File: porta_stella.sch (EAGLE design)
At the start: 85 parts, among them IC1 74LS00D, T1 2N3904, T2 PN3906, T3 PN3906, T4 PN3906, X1 SSW-112-02-G-Q

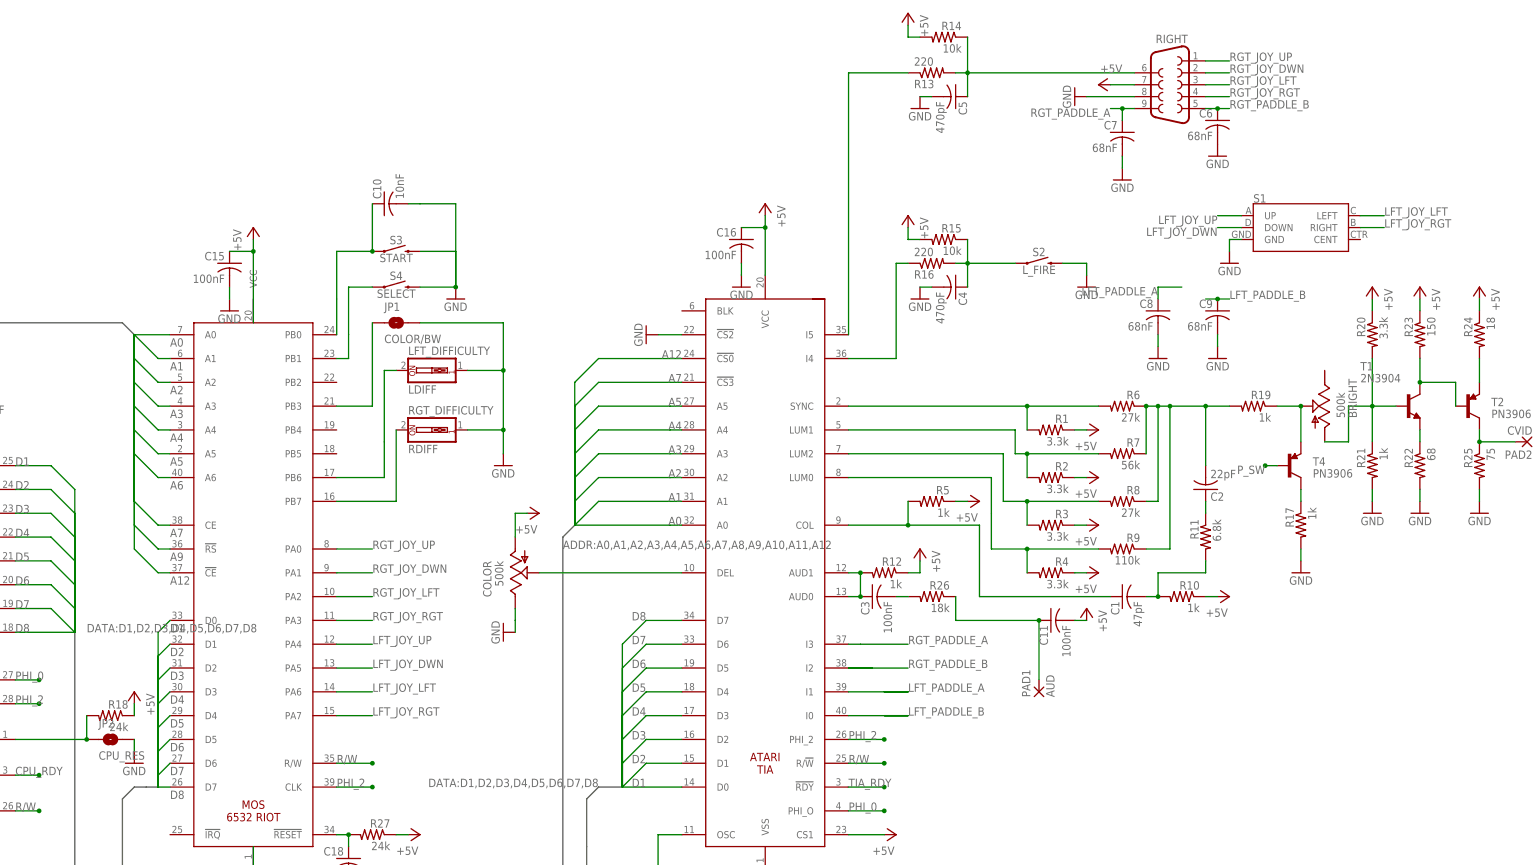
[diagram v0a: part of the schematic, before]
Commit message: more layout work for handheld
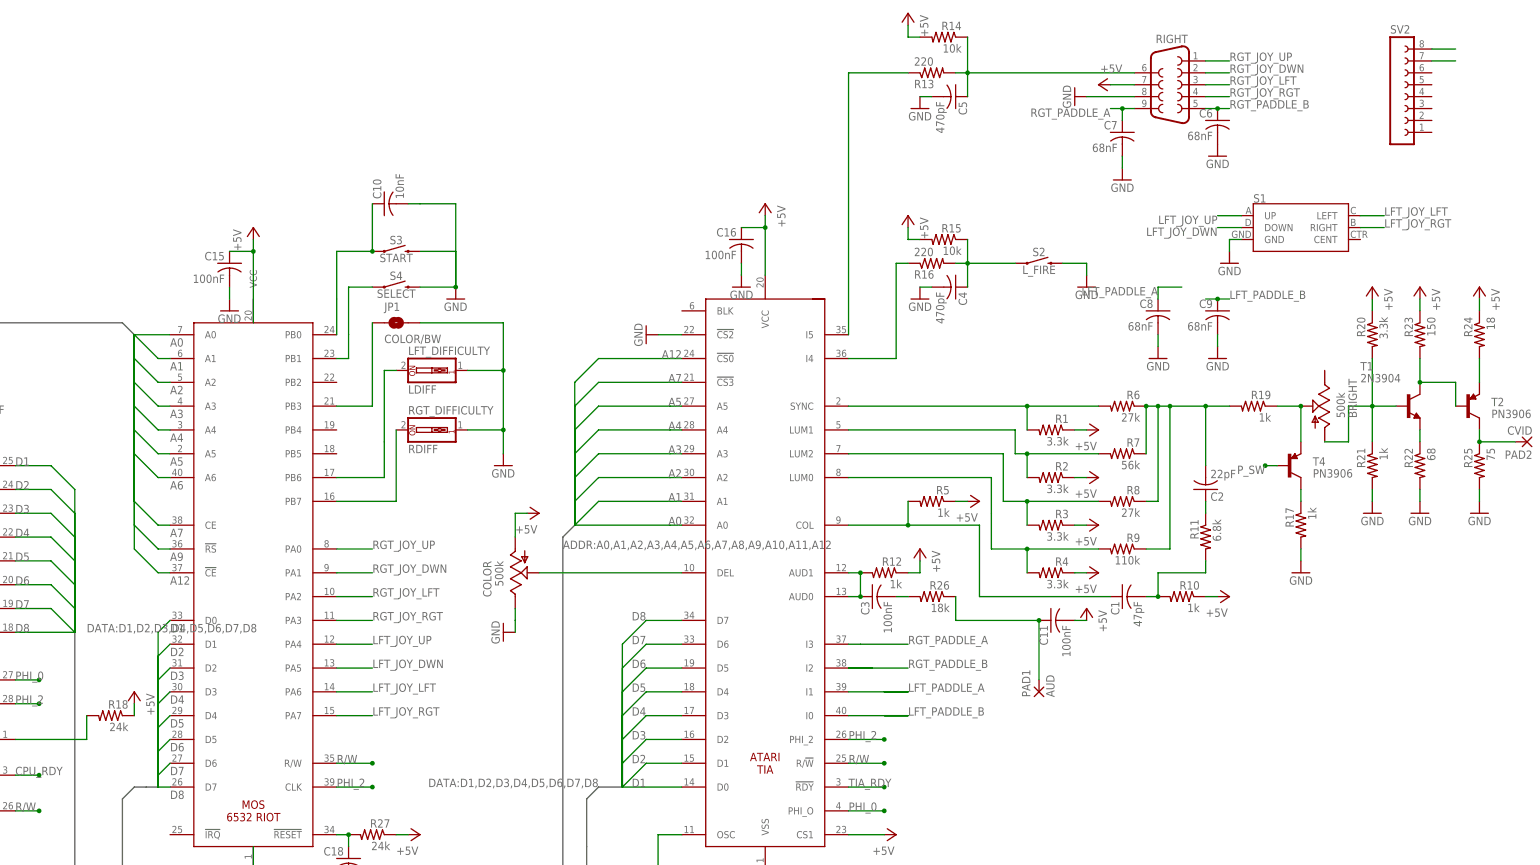
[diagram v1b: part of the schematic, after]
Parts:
- removed JP2: CPU_RES, SparkFun-Jumpers:JUMPER-SMT_2_NO_NO-SILK
- added SV2: (no value), con-lsta:FE08-1
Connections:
- new net N$37: SV2.8
- new net N$41: SV2.7
- net GND: no longer JP2.2
- net N$23: no longer JP2.1
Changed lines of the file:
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@@
 <part name="LDIFF" library="special" library_urn="urn:adsk.eagle:library:367" deviceset="SW_DIP-1" device="" package3d_urn="urn:adsk.eagle:package:26661/1" value="LFT_DIFFICULTY"/>
 <part name="GND17" library="supply1" library_urn="urn:adsk.eagle:library:371" deviceset="GND" device=""/>
-<part name="JP2" library="SparkFun-Jumpers" library_urn="urn:adsk.eagle:library:528" deviceset="JUMPER-SMT_2_NO" device="_NO-SILK" package3d_urn="urn:adsk.eagle:package:39277/1" value="CPU_RES"/>
-<part name="GND18" library="supply1" library_urn="urn:adsk.eagle:library:371" deviceset="GND" device=""/>
 <part name="R18" library="resistor" library_urn="urn:adsk.eagle:library:348" deviceset="R-US_" device="M0805" package3d_urn="urn:adsk.eagle:package:26079/1" value="24k"/>
 <part name="P+14" library="supply1" library_urn="urn:adsk.eagle:library:371" deviceset="+5V" device=""/>
@@
 <part name="PAD1" library="wirepad" library_urn="urn:adsk.eagle:library:412" deviceset="WIREPAD" device="4,16O1,6" package3d_urn="urn:adsk.eagle:package:30843/1" value="AUD"/>
 <part name="PAD2" library="wirepad" library_urn="urn:adsk.eagle:library:412" deviceset="WIREPAD" device="4,16O1,6" package3d_urn="urn:adsk.eagle:package:30843/1" value="CVID"/>
+<part name="SV2" library="con-lsta" library_urn="urn:adsk.eagle:library:161" deviceset="FE08-1" device="" package3d_urn="urn:adsk.eagle:package:8194/1"/>
 </parts>
 <sheets>
@@
 <instance part="LDIFF" gate="G$1" x="78.74" y="76.2" rot="MR180"/>
 <instance part="GND17" gate="1" x="93.98" y="55.88"/>
-<instance part="JP2" gate="G$1" x="10.16" y="-2.54"/>
-<instance part="GND18" gate="1" x="15.24" y="-7.62"/>
 <instance part="R18" gate="G$1" x="10.16" y="2.54" rot="MR0"/>
 <instance part="P+14" gate="1" x="15.24" y="7.62" rot="MR0"/>
@@
 <instance part="PAD1" gate="G$1" x="208.28" y="7.62" rot="R90"/>
 <instance part="PAD2" gate="G$1" x="312.42" y="60.96" rot="R180"/>
+<instance part="SV2" gate="G$1" x="284.48" y="134.62"/>
 </instances>
 <busses>
@@
 </segment>
 <segment>
-<pinref part="JP2" gate="G$1" pin="2"/>
-<pinref part="GND18" gate="1" pin="GND"/>
-<wire x1="15.24" y1="-5.08" x2="15.24" y2="-2.54" width="0.1524" layer="91"/>
-</segment>
-<segment>
 <pinref part="6532" gate="G$1" pin="VSS"/>
 <pinref part="GND1" gate="1" pin="GND"/>
@@
 <segment>
 <pinref part="6507" gate="G$1" pin="!RES"/>
-<pinref part="JP2" gate="G$1" pin="1"/>
 <wire x1="5.08" y1="-2.54" x2="-10.16" y2="-2.54" width="0.1524" layer="91"/>
 <pinref part="R18" gate="G$1" pin="2"/>
 <wire x1="5.08" y1="-2.54" x2="5.08" y2="2.54" width="0.1524" layer="91"/>
-<junction x="5.08" y="-2.54"/>
 </segment>
 </net>
@@
 </segment>
 </net>
+<net name="N$37" class="0">
+<segment>
+<pinref part="SV2" gate="G$1" pin="8"/>
+<wire x1="292.1" y1="144.78" x2="297.18" y2="144.78" width="0.1524" layer="91"/>
+</segment>
+</net>
+<net name="N$41" class="0">
+<segment>
+<pinref part="SV2" gate="G$1" pin="7"/>
+<wire x1="292.1" y1="142.24" x2="297.18" y2="142.24" width="0.1524" layer="91"/>
+</segment>
+</net>
